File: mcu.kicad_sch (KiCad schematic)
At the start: 66 parts, among them J10 PinHeader_2x10_P1.27mm_SMD_Sh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, SW5 SW_B3U-1000P_SMD, SW6 CAS-120TA, U1 STM32H753ZIT6, Y1 Resonator_32.768kHz_ECX-31B, Y2 Oscillator_25MHz_ESC_2016MV

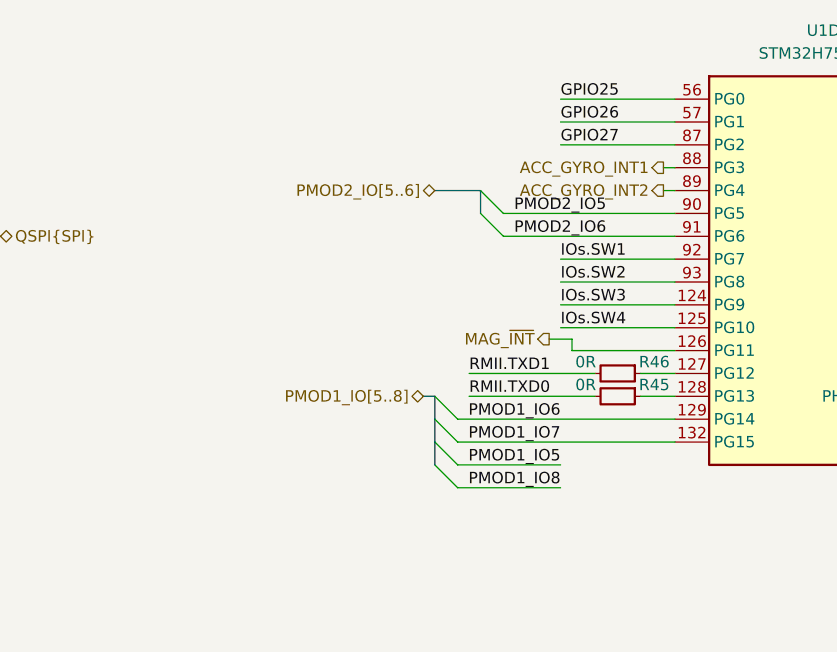
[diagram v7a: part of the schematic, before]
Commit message: [#95036] Fix hierarchical ports directions, add CAN termination jumper
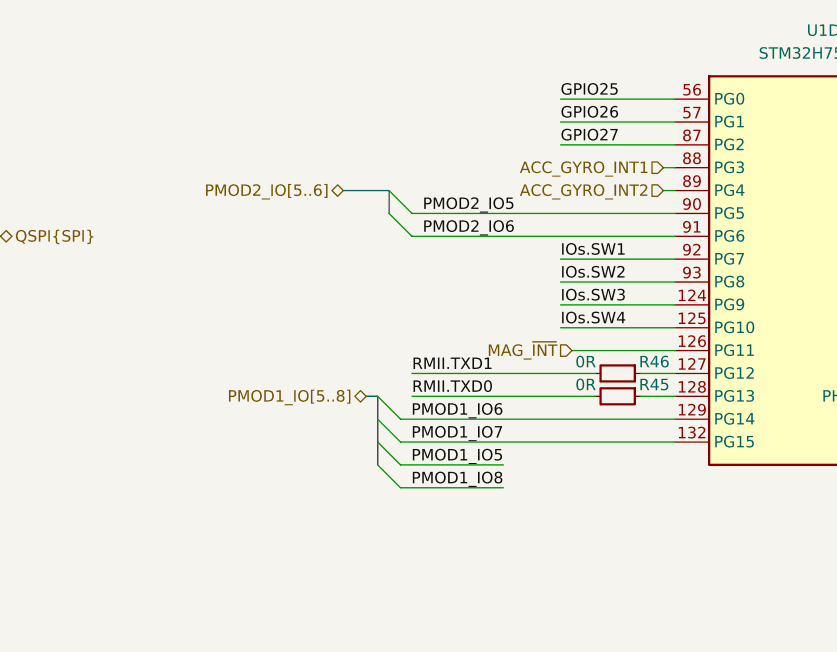
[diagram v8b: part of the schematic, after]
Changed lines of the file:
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@@
 	)
 	(bus_entry
-		(at 290.83 222.25)
+		(at 284.48 222.25)
 		(size 2.54 2.54)
 		(stroke
@@
 	)
 	(bus_entry
-		(at 290.83 214.63)
+		(at 284.48 214.63)
 		(size 2.54 2.54)
 		(stroke
@@
 	)
 	(bus_entry
-		(at 295.91 194.31)
+		(at 285.75 194.31)
 		(size 2.54 2.54)
 		(stroke
@@
 	)
 	(bus_entry
-		(at 295.91 191.77)
+		(at 285.75 191.77)
 		(size 2.54 2.54)
 		(stroke
@@
 	)
 	(bus_entry
-		(at 290.83 219.71)
+		(at 284.48 219.71)
 		(size 2.54 2.54)
 		(stroke
@@
 	)
 	(bus_entry
-		(at 290.83 217.17)
+		(at 284.48 217.17)
 		(size 2.54 2.54)
 		(stroke
@@
 	(bus
 		(pts
-			(xy 290.83 217.17) (xy 290.83 219.71)
+			(xy 284.48 217.17) (xy 284.48 219.71)
 		)
 		(stroke
@@
 	(wire
 		(pts
-			(xy 298.45 196.85) (xy 317.5 196.85)
+			(xy 288.29 196.85) (xy 317.5 196.85)
 		)
 		(stroke
@@
 	(wire
 		(pts
-			(xy 308.61 214.63) (xy 294.64 214.63)
+			(xy 288.29 214.63) (xy 308.61 214.63)
 		)
 		(stroke
@@
 	(bus
 		(pts
-			(xy 295.91 191.77) (xy 295.91 194.31)
+			(xy 285.75 191.77) (xy 285.75 194.31)
 		)
 		(stroke
@@
 	(wire
 		(pts
-			(xy 293.37 217.17) (xy 317.5 217.17)
+			(xy 287.02 217.17) (xy 317.5 217.17)
 		)
 		(stroke
@@
 	(bus
 		(pts
-			(xy 290.83 214.63) (xy 290.83 217.17)
+			(xy 284.48 214.63) (xy 284.48 217.17)
 		)
 		(stroke
@@
 	(wire
 		(pts
-			(xy 293.37 222.25) (xy 304.8 222.25)
+			(xy 287.02 222.25) (xy 298.45 222.25)
 		)
 		(stroke
@@
 	(bus
 		(pts
-			(xy 290.83 191.77) (xy 295.91 191.77)
+			(xy 280.67 191.77) (xy 285.75 191.77)
 		)
 		(stroke
@@
 	(wire
 		(pts
-			(xy 298.45 194.31) (xy 317.5 194.31)
+			(xy 288.29 194.31) (xy 317.5 194.31)
 		)
 		(stroke
@@
 	(wire
 		(pts
-			(xy 303.53 208.28) (xy 306.07 208.28)
-		)
-		(stroke
-			(width 0)
-			(type default)
-		)
-	)
-	(wire
-		(pts
 			(xy 138.43 149.86) (xy 139.7 149.86)
 		)
@@
 	(wire
 		(pts
-			(xy 306.07 208.28) (xy 306.07 209.55)
-		)
-		(stroke
-			(width 0)
-			(type default)
-		)
-	)
-	(wire
-		(pts
 			(xy 364.49 114.3) (xy 364.49 111.76)
 		)
@@
 	(wire
 		(pts
-			(xy 304.8 224.79) (xy 293.37 224.79)
+			(xy 298.45 224.79) (xy 287.02 224.79)
 		)
 		(stroke
@@
 	(wire
 		(pts
-			(xy 293.37 219.71) (xy 317.5 219.71)
+			(xy 287.02 219.71) (xy 317.5 219.71)
 		)
 		(stroke
@@
 	(wire
 		(pts
-			(xy 306.07 209.55) (xy 317.5 209.55)
-		)
-		(stroke
-			(width 0)
-			(type default)
-		)
-	)
-	(wire
-		(pts
 			(xy 355.6 67.31) (xy 355.6 68.58)
 		)
@@
 		)
 	)
+	(wire
+		(pts
+			(xy 306.07 209.55) (xy 317.5 209.55)
+		)
+		(stroke
+			(width 0)
+			(type default)
+		)
+	)
 	(bus
 		(pts
-			(xy 289.56 214.63) (xy 290.83 214.63)
+			(xy 283.21 214.63) (xy 284.48 214.63)
 		)
 		(stroke
@@
 	(wire
 		(pts
-			(xy 308.61 212.09) (xy 294.64 212.09)
+			(xy 288.29 212.09) (xy 308.61 212.09)
 		)
 		(stroke
@@
 	(bus
 		(pts
-			(xy 290.83 219.71) (xy 290.83 222.25)
+			(xy 284.48 219.71) (xy 284.48 222.25)
 		)
 		(stroke
@@
 	)
 	(label "PMOD2_IO6"
-		(at 309.88 196.85 180)
+		(at 299.72 196.85 180)
 		(effects
 			(font
@@
 	)
 	(label "PMOD2_IO5"
-		(at 309.88 194.31 180)
+		(at 299.72 194.31 180)
 		(effects
 			(font
@@
 	)
 	(label "PMOD1_IO8"
-		(at 304.8 224.79 180)
+		(at 298.45 224.79 180)
 		(effects
 			(font
@@
 	)
 	(label "PMOD1_IO6"
-		(at 304.8 217.17 180)
+		(at 298.45 217.17 180)
 		(effects
 			(font
@@
 	)
 	(label "RMII.TXD0"
-		(at 294.64 214.63 0)
+		(at 288.29 214.63 0)
 		(effects
 			(font
@@
 	)
 	(label "PMOD1_IO7"
-		(at 304.8 219.71 180)
+		(at 298.45 219.71 180)
 		(effects
 			(font
@@
 	)
 	(label "PMOD1_IO5"
-		(at 304.8 222.25 180)
+		(at 298.45 222.25 180)
 		(effects
 			(font
@@
 	)
 	(label "RMII.TXD1"
-		(at 294.64 212.09 0)
+		(at 288.29 212.09 0)
 		(effects
 			(font
@@
 	)
 	(hierarchical_label "ACC_GYRO_INT1"
-		(shape output)
+		(shape input)
 		(at 316.23 189.23 180)
 		(effects
@@
 	(hierarchical_label "PMOD2_IO[5..6]"
 		(shape bidirectional)
-		(at 290.83 191.77 180)
+		(at 280.67 191.77 180)
 		(effects
 			(font
@@
 	(hierarchical_label "PMOD1_IO[5..8]"
 		(shape bidirectional)
-		(at 289.56 214.63 180)
+		(at 283.21 214.63 180)
 		(effects
 			(font
@@
 	)
 	(hierarchical_label "MAG_~{INT}"
-		(shape output)
-		(at 303.53 208.28 180)
+		(shape input)
+		(at 306.07 209.55 180)
 		(effects
 			(font
@@
 	)
 	(hierarchical_label "ACC_GYRO_INT2"
-		(shape output)
+		(shape input)
 		(at 316.23 191.77 180)
 		(effects
